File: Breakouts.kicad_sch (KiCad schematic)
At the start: 16 parts, among them J1 Conn_01x08, J10 AudioJack3_Switch, J11 Conn_01x03, J12 Conn_01x03, J2 Conn_01x08, J3 Conn_01x08, J4 Conn_01x08, J5 Conn_02x04_Odd_Even, J6 Conn_01x06, J7 Conn_01x06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

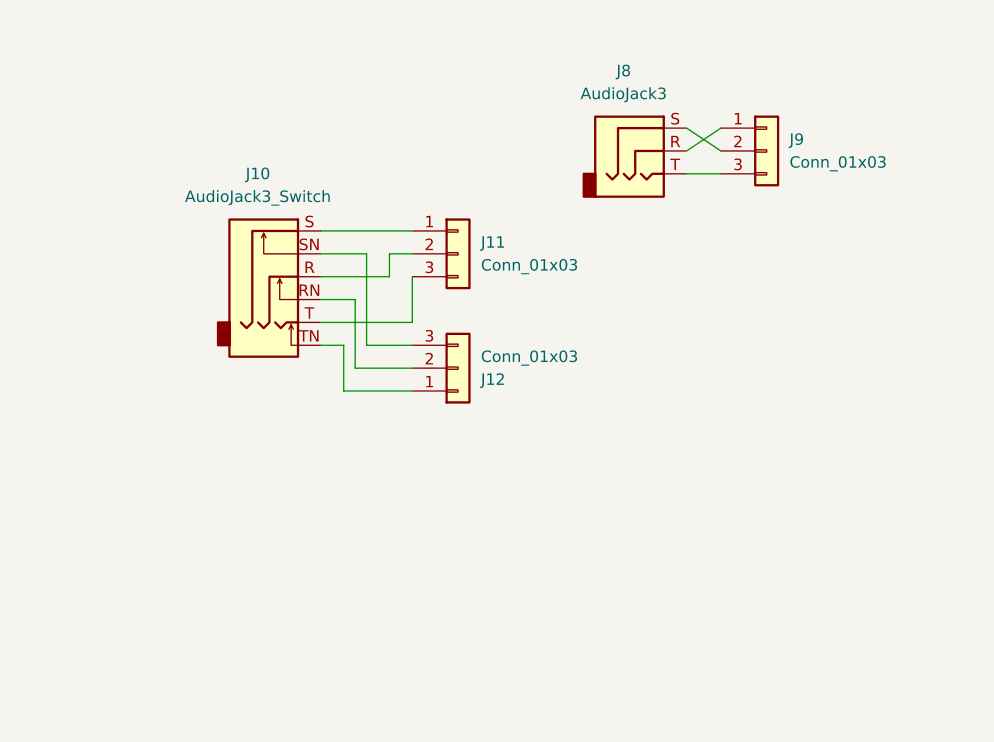
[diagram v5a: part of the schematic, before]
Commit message: Add barrel jack
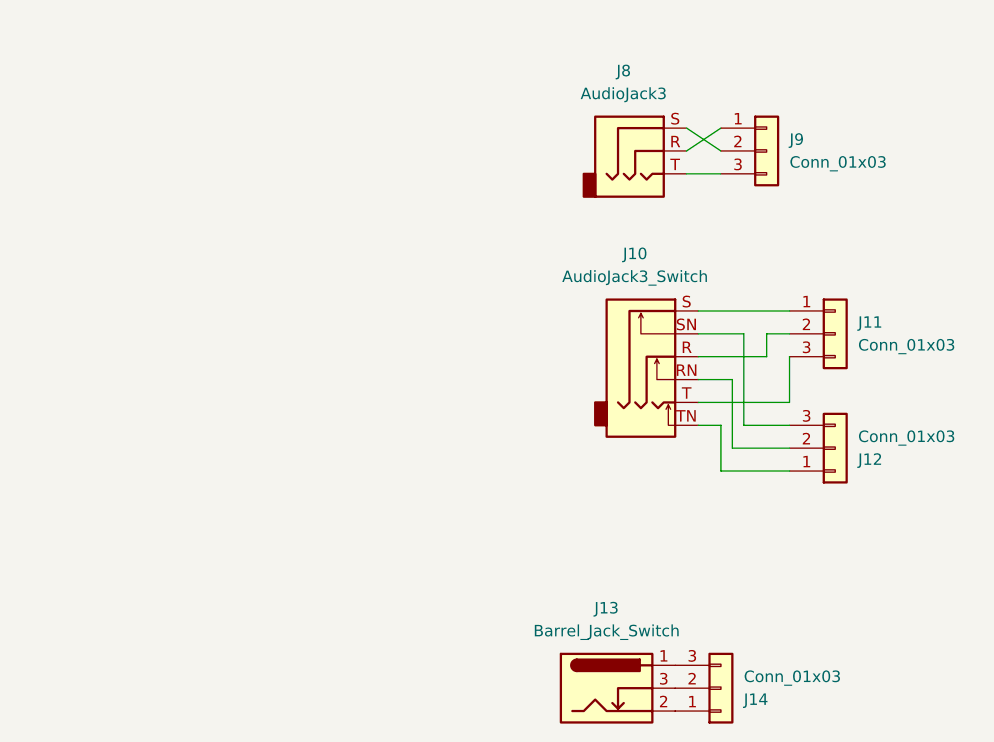
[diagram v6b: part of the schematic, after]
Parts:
- added J13: Barrel_Jack_Switch, Connector_BarrelJack:BarrelJack_GCT_DCJ200-10-A_Horizontal, symbol Connector:Barrel_Jack_Switch
- added J14: Conn_01x03, Connector_PinHeader_2.54mm:PinHeader_1x03_P2.54mm_Vertical_SMD_Pin1Left, symbol Connector_Generic:Conn_01x03
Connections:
- new net: J13.2, J14.1 (Pin_1)
- new net: J13.3, J14.2 (Pin_2)
- new net: J13.1, J14.3 (Pin_3)
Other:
- moved on the sheet: J10, J11, J12
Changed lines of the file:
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@@
     (stroke (width 0) (type default))
   )
-  (wire (pts (xy 214.63 102.87) (xy 217.17 102.87))
+  (wire (pts (xy 256.54 111.76) (xy 259.08 111.76))
     (stroke (width 0) (type default))
   )
@@
     (stroke (width 0) (type default))
   )
-  (wire (pts (xy 218.44 97.79) (xy 218.44 105.41))
-    (stroke (width 0) (type default))
-  )
-  (wire (pts (xy 222.25 92.71) (xy 222.25 95.25))
+  (wire (pts (xy 260.35 106.68) (xy 260.35 114.3))
+    (stroke (width 0) (type default))
+  )
+  (wire (pts (xy 264.16 101.6) (xy 264.16 104.14))
     (stroke (width 0) (type default))
   )
@@
     (stroke (width 0) (type default))
   )
-  (wire (pts (xy 218.44 105.41) (xy 224.79 105.41))
-    (stroke (width 0) (type default))
-  )
-  (wire (pts (xy 224.79 100.33) (xy 214.63 100.33))
-    (stroke (width 0) (type default))
-  )
-  (wire (pts (xy 222.25 95.25) (xy 214.63 95.25))
-    (stroke (width 0) (type default))
-  )
-  (wire (pts (xy 214.63 97.79) (xy 218.44 97.79))
-    (stroke (width 0) (type default))
-  )
-  (wire (pts (xy 217.17 107.95) (xy 224.79 107.95))
+  (wire (pts (xy 260.35 114.3) (xy 266.7 114.3))
+    (stroke (width 0) (type default))
+  )
+  (wire (pts (xy 266.7 109.22) (xy 256.54 109.22))
+    (stroke (width 0) (type default))
+  )
+  (wire (pts (xy 264.16 104.14) (xy 256.54 104.14))
+    (stroke (width 0) (type default))
+  )
+  (wire (pts (xy 256.54 106.68) (xy 260.35 106.68))
+    (stroke (width 0) (type default))
+  )
+  (wire (pts (xy 259.08 116.84) (xy 266.7 116.84))
     (stroke (width 0) (type default))
   )
@@
     (stroke (width 0) (type default))
   )
-  (wire (pts (xy 219.71 102.87) (xy 224.79 102.87))
+  (wire (pts (xy 261.62 111.76) (xy 266.7 111.76))
     (stroke (width 0) (type default))
   )
@@
     (stroke (width 0) (type default))
   )
-  (wire (pts (xy 224.79 92.71) (xy 222.25 92.71))
+  (wire (pts (xy 266.7 101.6) (xy 264.16 101.6))
     (stroke (width 0) (type default))
   )
@@
     (stroke (width 0) (type default))
   )
-  (wire (pts (xy 224.79 95.25) (xy 224.79 100.33))
+  (wire (pts (xy 266.7 104.14) (xy 266.7 109.22))
     (stroke (width 0) (type default))
   )
@@
     (stroke (width 0) (type default))
   )
-  (wire (pts (xy 224.79 90.17) (xy 214.63 90.17))
+  (wire (pts (xy 266.7 99.06) (xy 256.54 99.06))
     (stroke (width 0) (type default))
   )
@@
     (stroke (width 0) (type default))
   )
-  (wire (pts (xy 219.71 92.71) (xy 219.71 102.87))
+  (wire (pts (xy 261.62 101.6) (xy 261.62 111.76))
     (stroke (width 0) (type default))
   )
@@
     (stroke (width 0) (type default))
   )
-  (wire (pts (xy 217.17 102.87) (xy 217.17 107.95))
-    (stroke (width 0) (type default))
-  )
-  (wire (pts (xy 214.63 92.71) (xy 219.71 92.71))
+  (wire (pts (xy 259.08 111.76) (xy 259.08 116.84))
+    (stroke (width 0) (type default))
+  )
+  (wire (pts (xy 256.54 101.6) (xy 261.62 101.6))
     (stroke (width 0) (type default))
   )
@@
     )
   )
-  (symbol (lib_id "Connector_Generic:Conn_01x03") (at 229.87 92.71 0) (unit 1)
+  (symbol (lib_id "Connector_Generic:Conn_01x03") (at 271.78 101.6 0) (unit 1)
     (in_bom yes) (on_board yes) (dnp no)
-    (property "Reference" "J11" (at 232.41 91.44 0)
-      (effects (font (size 1.27 1.27)) (justify left))
-    )
-    (property "Value" "Conn_01x03" (at 232.41 93.98 0)
-      (effects (font (size 1.27 1.27)) (justify left))
-    )
-    (property "Footprint" "Connector_PinHeader_2.54mm:PinHeader_1x03_P2.54mm_Vertical_SMD_Pin1Left" (at 229.87 92.71 0)
-      (effects (font (size 1.27 1.27)) hide)
-    )
-    (property "Datasheet" "~" (at 229.87 92.71 0)
+    (property "Reference" "J11" (at 274.32 100.33 0)
+      (effects (font (size 1.27 1.27)) (justify left))
+    )
+    (property "Value" "Conn_01x03" (at 274.32 102.87 0)
+      (effects (font (size 1.27 1.27)) (justify left))
+    )
+    (property "Footprint" "Connector_PinHeader_2.54mm:PinHeader_1x03_P2.54mm_Vertical_SMD_Pin1Left" (at 271.78 101.6 0)
+      (effects (font (size 1.27 1.27)) hide)
+    )
+    (property "Datasheet" "~" (at 271.78 101.6 0)
       (effects (font (size 1.27 1.27)) hide)
     )
@@
     )
   )
+  (symbol (lib_id "Connector_Generic:Conn_01x03") (at 259.08 140.97 0) (mirror x) (unit 1)
+    (in_bom yes) (on_board yes) (dnp no)
+    (property "Reference" "J14" (at 261.62 142.24 0)
+      (effects (font (size 1.27 1.27)) (justify left))
+    )
+    (property "Value" "Conn_01x03" (at 261.62 139.7 0)
+      (effects (font (size 1.27 1.27)) (justify left))
+    )
+    (property "Footprint" "Connector_PinHeader_2.54mm:PinHeader_1x03_P2.54mm_Vertical_SMD_Pin1Left" (at 259.08 140.97 0)
+      (effects (font (size 1.27 1.27)) hide)
+    )
+    (property "Datasheet" "~" (at 259.08 140.97 0)
+      (effects (font (size 1.27 1.27)) hide)
+    )
+    (pin "1")
+    (pin "2")
+    (pin "3")
+    (instances
+      (project "Breakouts"
+        (path "/7ebf650a-1c0b-4d71-8ef1-c883cde2ac89"
+          (reference "J14") (unit 1)
+        )
+      )
+    )
+  )
   (symbol (lib_id "Connector_Generic:Conn_01x08") (at 84.455 36.195 0) (mirror y) (unit 1)
     (in_bom yes) (on_board yes) (dnp no) (fields_autoplaced)
@@
     )
   )
-  (symbol (lib_id "Connector_Generic:Conn_01x03") (at 229.87 105.41 0) (mirror x) (unit 1)
+  (symbol (lib_id "Connector:Barrel_Jack_Switch") (at 246.38 140.97 0) (unit 1)
+    (in_bom yes) (on_board yes) (dnp no) (fields_autoplaced)
+    (property "Reference" "J13" (at 246.38 132.08 0)
+      (effects (font (size 1.27 1.27)))
+    )
+    (property "Value" "Barrel_Jack_Switch" (at 246.38 134.62 0)
+      (effects (font (size 1.27 1.27)))
+    )
+    (property "Footprint" "Connector_BarrelJack:BarrelJack_GCT_DCJ200-10-A_Horizontal" (at 247.65 141.986 0)
+      (effects (font (size 1.27 1.27)) hide)
+    )
+    (property "Datasheet" "~" (at 247.65 141.986 0)
+      (effects (font (size 1.27 1.27)) hide)
+    )
+    (pin "1")
+    (pin "3")
+    (pin "2")
+    (instances
+      (project "Breakouts"
+        (path "/7ebf650a-1c0b-4d71-8ef1-c883cde2ac89"
+          (reference "J13") (unit 1)
+        )
+      )
+    )
+  )
+  (symbol (lib_id "Connector_Generic:Conn_01x03") (at 271.78 114.3 0) (mirror x) (unit 1)
     (in_bom yes) (on_board yes) (dnp no)
-    (property "Reference" "J12" (at 232.41 106.68 0)
-      (effects (font (size 1.27 1.27)) (justify left))
-    )
-    (property "Value" "Conn_01x03" (at 232.41 104.14 0)
-      (effects (font (size 1.27 1.27)) (justify left))
-    )
-    (property "Footprint" "Connector_PinHeader_2.54mm:PinHeader_1x03_P2.54mm_Vertical_SMD_Pin1Left" (at 229.87 105.41 0)
-      (effects (font (size 1.27 1.27)) hide)
-    )
-    (property "Datasheet" "~" (at 229.87 105.41 0)
+    (property "Reference" "J12" (at 274.32 115.57 0)
+      (effects (font (size 1.27 1.27)) (justify left))
+    )
+    (property "Value" "Conn_01x03" (at 274.32 113.03 0)
+      (effects (font (size 1.27 1.27)) (justify left))
+    )
+    (property "Footprint" "Connector_PinHeader_2.54mm:PinHeader_1x03_P2.54mm_Vertical_SMD_Pin1Left" (at 271.78 114.3 0)
+      (effects (font (size 1.27 1.27)) hide)
+    )
+    (property "Datasheet" "~" (at 271.78 114.3 0)
       (effects (font (size 1.27 1.27)) hide)
     )
@@
     )
   )
-  (symbol (lib_id "Connector_Audio:AudioJack3_Switch") (at 209.55 95.25 0) (unit 1)
-    (in_bom yes) (on_board yes) (dnp no) (fields_autoplaced)
-    (property "Reference" "J10" (at 207.645 83.82 0)
-      (effects (font (size 1.27 1.27)))
-    )
-    (property "Value" "AudioJack3_Switch" (at 207.645 86.36 0)
-      (effects (font (size 1.27 1.27)))
-    )
-    (property "Footprint" "Connector_Audio:Jack_6.35mm_Neutrik_NMJ6HFD2_Horizontal" (at 209.55 95.25 0)
-      (effects (font (size 1.27 1.27)) hide)
-    )
-    (property "Datasheet" "~" (at 209.55 95.25 0)
-      (effects (font (size 1.27 1.27)) hide)
-    )
+  (symbol (lib_id "Connector_Audio:AudioJack3_Switch") (at 251.46 104.14 0) (unit 1)
+    (in_bom yes) (on_board yes) (dnp no) (fields_autoplaced)
+    (property "Reference" "J10" (at 249.555 92.71 0)
+      (effects (font (size 1.27 1.27)))
+    )
+    (property "Value" "AudioJack3_Switch" (at 249.555 95.25 0)
+      (effects (font (size 1.27 1.27)))
+    )
+    (property "Footprint" "Connector_Audio:Jack_6.35mm_Neutrik_NMJ6HFD2_Horizontal" (at 251.46 104.14 0)
+      (effects (font (size 1.27 1.27)) hide)
+    )
+    (property "Datasheet" "~" (at 251.46 104.14 0)
+      (effects (font (size 1.27 1.27)) hide)
+    )

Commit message: Add ULN2003 breakout
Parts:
- added J15, J16: Conn_01x08, Connector_PinHeader_2.00mm:PinHeader_1x08_P2.00mm_Vertical, symbol Connector_Generic:Conn_01x08
- added U4: ULN2003, Package_SO:SOIC-16W_5.3x10.2mm_P1.27mm, symbol Transistor_Array:ULN2003
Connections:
- new net: J15.1 (Pin_1), U4.1 (I1)
- new net: J16.7 (Pin_7), U4.10 (O7)
- new net: J16.6 (Pin_6), U4.11 (O6)
- new net: J16.5 (Pin_5), U4.12 (O5)
- new net: J16.4 (Pin_4), U4.13 (O4)
- new net: J16.3 (Pin_3), U4.14 (O3)
- new net: J16.2 (Pin_2), U4.15 (O2)
- new net: J16.1 (Pin_1), U4.16 (O1)
- new net: J15.2 (Pin_2), U4.2 (I2)
- new net: J15.3 (Pin_3), U4.3 (I3)
- new net: J15.4 (Pin_4), U4.4 (I4)
- new net: J15.5 (Pin_5), U4.5 (I5)
- new net: J15.6 (Pin_6), U4.6 (I6)
- new net: J15.7 (Pin_7), U4.7 (I7)
- new net: J15.8 (Pin_8), U4.8 (GND)
- new net: J16.8 (Pin_8), U4.9 (COM)
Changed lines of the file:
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@@
   (no_connect (at 266.7 27.94))
   (no_connect (at 198.12 59.055))
+  (wire (pts (xy 184.15 118.11) (xy 173.99 118.11))
+    (stroke (width 0) (type default))
+  )
   (wire (pts (xy 259.08 29.21) (xy 259.08 27.94))
     (stroke (width 0) (type default))
@@
     (stroke (width 0) (type default))
   )
+  (wire (pts (xy 173.99 92.71) (xy 184.15 92.71))
+    (stroke (width 0) (type default))
+  )
   (wire (pts (xy 260.35 106.68) (xy 260.35 114.3))
     (stroke (width 0) (type default))
@@
     (stroke (width 0) (type default))
   )
+  (wire (pts (xy 153.67 118.11) (xy 153.67 115.57))
+    (stroke (width 0) (type default))
+  )
   (wire (pts (xy 55.88 86.36) (xy 63.5 86.36))
     (stroke (width 0) (type default))
@@
     (stroke (width 0) (type default))
   )
+  (wire (pts (xy 173.99 118.11) (xy 173.99 115.57))
+    (stroke (width 0) (type default))
+  )
   (wire (pts (xy 271.78 33.02) (xy 276.86 33.02))
     (stroke (width 0) (type default))
@@
     (stroke (width 0) (type default))
   )
+  (wire (pts (xy 184.15 92.71) (xy 184.15 118.11))
+    (stroke (width 0) (type default))
+  )
   (wire (pts (xy 255.27 78.74) (xy 259.08 81.28))
+    (stroke (width 0) (type default))
+  )
+  (wire (pts (xy 163.83 118.11) (xy 153.67 118.11))
     (stroke (width 0) (type default))
   )
@@
     )
   )
+  (symbol (lib_id "Transistor_Array:ULN2003") (at 163.83 102.87 0) (unit 1)
+    (in_bom yes) (on_board yes) (dnp no) (fields_autoplaced)
+    (property "Reference" "U4" (at 163.83 85.09 0)
+      (effects (font (size 1.27 1.27)))
+    )
+    (property "Value" "ULN2003" (at 163.83 87.63 0)
+      (effects (font (size 1.27 1.27)))
+    )
+    (property "Footprint" "Package_SO:SOIC-16W_5.3x10.2mm_P1.27mm" (at 165.1 116.84 0)
+      (effects (font (size 1.27 1.27)) (justify left) hide)
+    )
+    (property "Datasheet" "http://www.ti.com/lit/ds/symlink/uln2003a.pdf" (at 166.37 107.95 0)
+      (effects (font (size 1.27 1.27)) hide)
+    )
+    (pin "11")
+    (pin "14")
+    (pin "12")
+    (pin "7")
+    (pin "15")
+    (pin "3")
+    (pin "10")
+    (pin "16")
+    (pin "4")
+    (pin "6")
+    (pin "5")
+    (pin "8")
+    (pin "1")
+    (pin "13")
+    (pin "2")
+    (pin "9")
+    (instances
+      (project "Breakouts"
+        (path "/7ebf650a-1c0b-4d71-8ef1-c883cde2ac89"
+          (reference "U4") (unit 1)
+        )
+      )
+    )
+  )
+  (symbol (lib_id "Connector_Generic:Conn_01x08") (at 148.59 105.41 0) (mirror y) (unit 1)
+    (in_bom yes) (on_board yes) (dnp no) (fields_autoplaced)
+    (property "Reference" "J15" (at 148.59 91.44 0)
+      (effects (font (size 1.27 1.27)))
+    )
+    (property "Value" "Conn_01x08" (at 148.59 93.98 0)
+      (effects (font (size 1.27 1.27)))
+    )
+    (property "Footprint" "Connector_PinHeader_2.00mm:PinHeader_1x08_P2.00mm_Vertical" (at 148.59 105.41 0)
+      (effects (font (size 1.27 1.27)) hide)
+    )
+    (property "Datasheet" "~" (at 148.59 105.41 0)
+      (effects (font (size 1.27 1.27)) hide)
+    )
+    (pin "6")
+    (pin "5")
+    (pin "3")
+    (pin "8")
+    (pin "2")
+    (pin "7")
+    (pin "4")
+    (pin "1")
+    (instances
+      (project "Breakouts"
+        (path "/7ebf650a-1c0b-4d71-8ef1-c883cde2ac89"
+          (reference "J15") (unit 1)
+        )
+      )
+    )
+  )
   (symbol (lib_id "Connector_Generic:Conn_01x03") (at 259.08 140.97 0) (mirror x) (unit 1)
     (in_bom yes) (on_board yes) (dnp no)
@@
         )
       )
+    )
+  )
+  (symbol (lib_id "Connector_Generic:Conn_01x08") (at 179.07 105.41 0) (unit 1)
+    (in_bom yes) (on_board yes) (dnp no)
+    (property "Reference" "J16" (at 179.07 91.44 0)
+      (effects (font (size 1.27 1.27)))
+    )
+    (property "Value" "Conn_01x08" (at 179.07 93.98 0)
+      (effects (font (size 1.27 1.27)))
+    )
+    (property "Footprint" "Connector_PinHeader_2.00mm:PinHeader_1x08_P2.00mm_Vertical" (at 179.07 105.41 0)
+      (effects (font (size 1.27 1.27)) hide)
+    )
+    (property "Datasheet" "~" (at 179.07 105.41 0)
+      (effects (font (size 1.27 1.27)) hide)
+    )
+    (pin "6")
+    (pin "5")
+    (pin "3")
+    (pin "8")
+    (pin "2")
+    (pin "7")
+    (pin "4")
+    (pin "1")
+    (instances
+      (project "Breakouts"
+        (path "/7ebf650a-1c0b-4d71-8ef1-c883cde2ac89"
+          (reference "J16") (unit 1)
+        )
+      )

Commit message: Add ULN2003 breakout with copper pour
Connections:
- net GND: now also J15.8 (Pin_8), U4.8 (GND)
- net POWx: now reaches J16.8 (Pin_8), U4.9 (COM)
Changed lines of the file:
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@@
   (junction (at 55.88 86.36) (diameter 0) (color 0 0 0 0)
+  )
+  (junction (at 160.02 118.11) (diameter 0) (color 0 0 0 0)
   )
   (no_connect (at 193.04 59.055))
@@
     (stroke (width 0) (type default))
   )
+  (wire (pts (xy 160.02 118.11) (xy 153.67 118.11))
+    (stroke (width 0) (type default))
+  )
   (wire (pts (xy 63.5 78.74) (xy 57.15 78.74))
     (stroke (width 0) (type default))
@@
     (stroke (width 0) (type default))
   )
-  (wire (pts (xy 163.83 118.11) (xy 153.67 118.11))
+  (wire (pts (xy 163.83 118.11) (xy 160.02 118.11))
     (stroke (width 0) (type default))
   )
@@
   (wire (pts (xy 256.54 101.6) (xy 261.62 101.6))
     (stroke (width 0) (type default))
+  )
+  (global_label "POWx" (shape input) (at 175.26 92.71 90) (fields_autoplaced)
+    (effects (font (size 1.27 1.27)) (justify left))
+    (property "Intersheetrefs" "${INTERSHEET_REFS}" (at 175.26 84.6448 90)
+      (effects (font (size 1.27 1.27)) (justify left) hide)
+    )
   )
   (symbol (lib_id "Connector_Generic:Conn_02x04_Odd_Even") (at 68.58 83.82 0) (mirror x) (unit 1)
@@
         )
       )
+    )
+  )
+  (symbol (lib_id "power:GND") (at 160.02 118.11 0) (unit 1)
+    (in_bom yes) (on_board yes) (dnp no) (fields_autoplaced)
+    (property "Reference" "#PWR02" (at 160.02 124.46 0)
+      (effects (font (size 1.27 1.27)) hide)
+    )
+    (property "Value" "GND" (at 160.02 123.19 0)
+      (effects (font (size 1.27 1.27)))
+    )
+    (property "Footprint" "" (at 160.02 118.11 0)
+      (effects (font (size 1.27 1.27)) hide)
+    )
+    (property "Datasheet" "" (at 160.02 118.11 0)
+      (effects (font (size 1.27 1.27)) hide)
+    )
+    (pin "1")
+    (instances
+      (project "Breakouts"
+        (path "/7ebf650a-1c0b-4d71-8ef1-c883cde2ac89"
+          (reference "#PWR02") (unit 1)
+        )
+      )
